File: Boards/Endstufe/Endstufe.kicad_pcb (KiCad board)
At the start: 2 copper layers, 163.6 x 110.2 mm, 60 parts, among them J1 HV In, J2 Relais, J3 NF_In, K1 G6E, P2 Trafo, P4 6V3_AC, P5 Trafo_GK, P6 6V3_DC, P7 VSup1, P8 Bias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

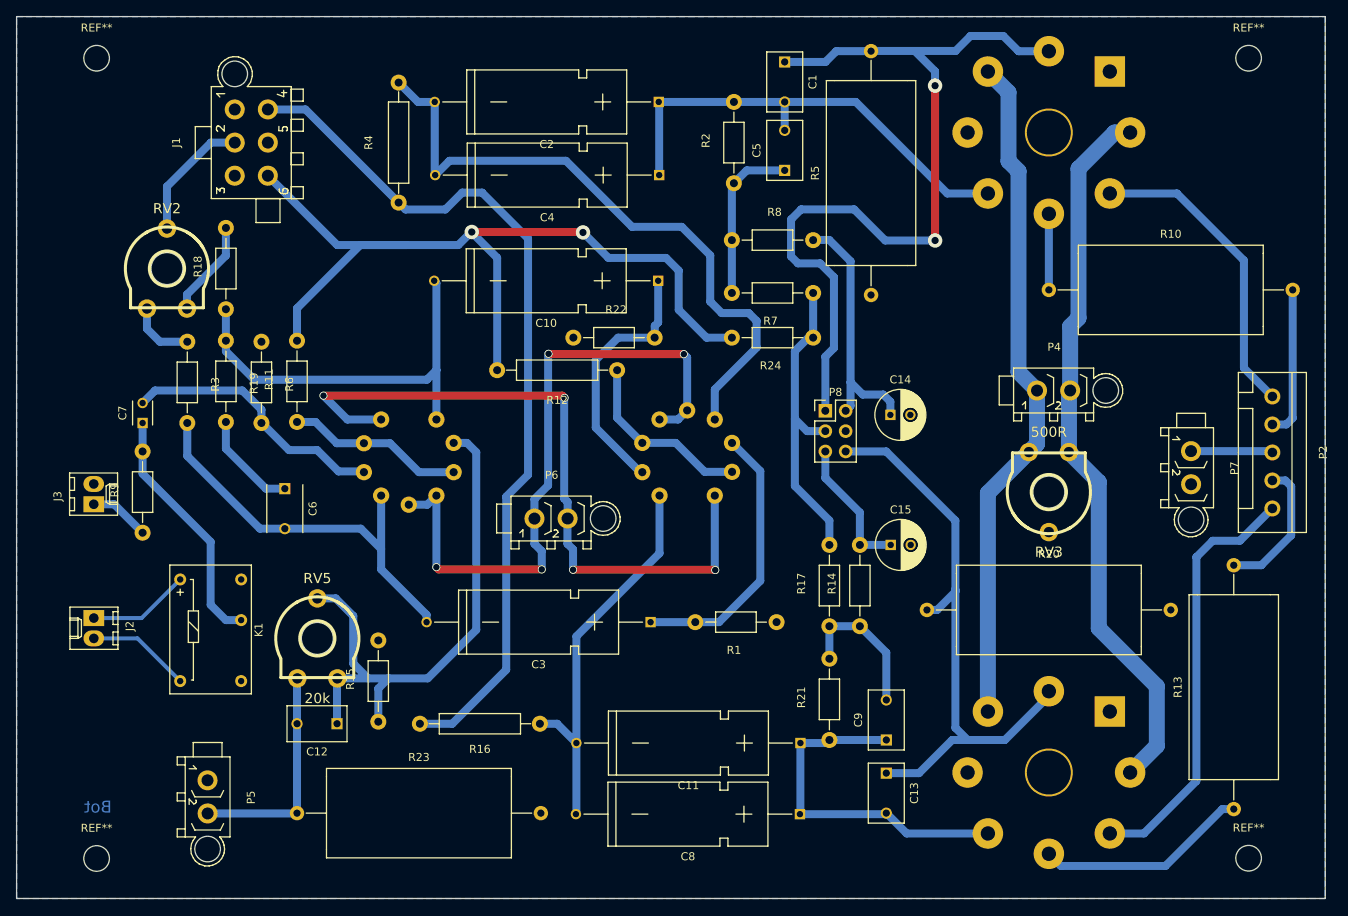
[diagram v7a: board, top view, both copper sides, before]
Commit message: Converted to Kicad 5.1 and Layout changes
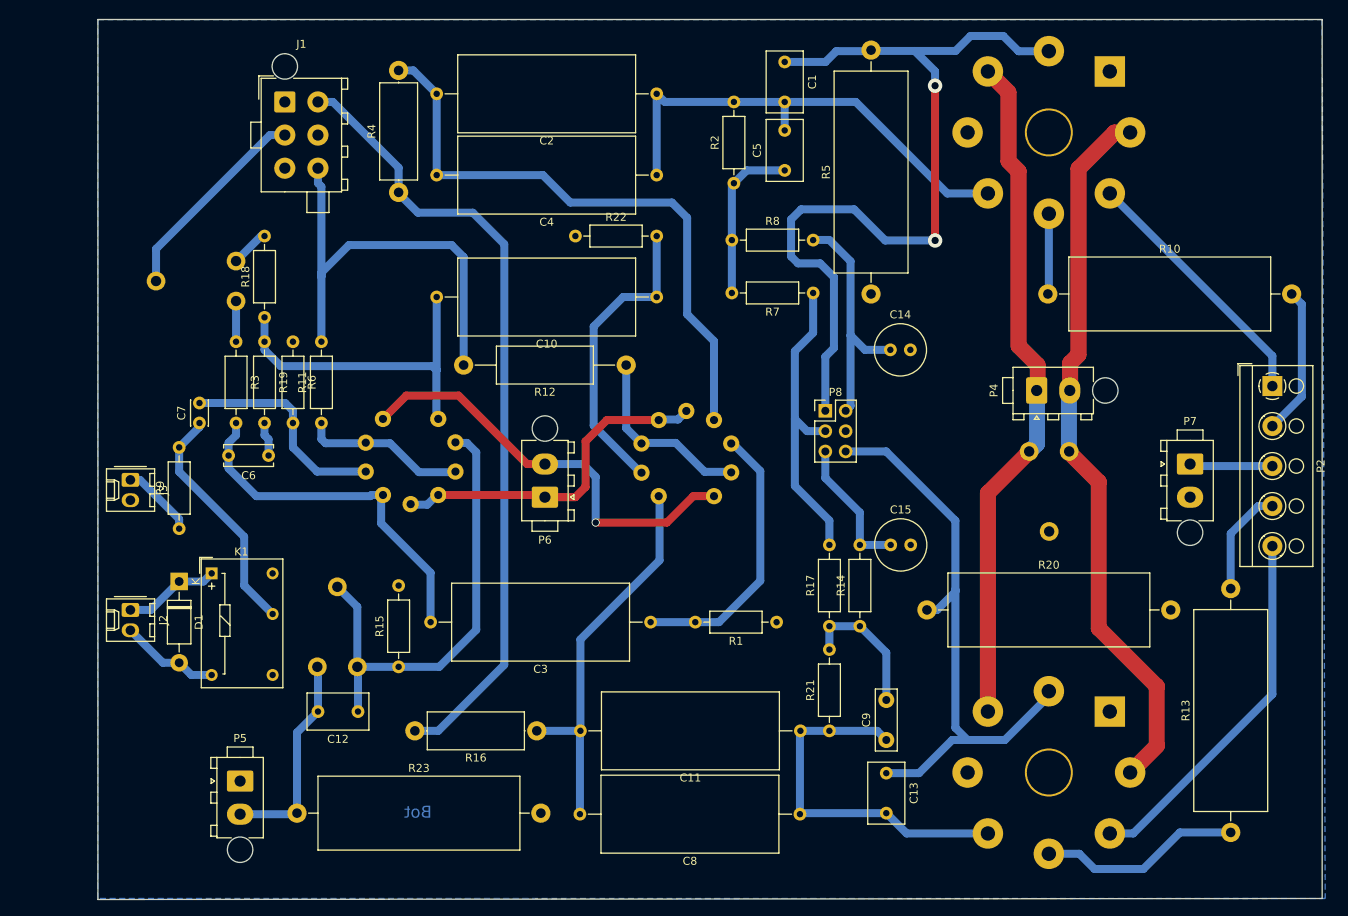
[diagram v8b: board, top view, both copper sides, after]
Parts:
- removed R24: 30k, Resistors_ThroughHole:Resistor_Horizontal_RM10mm
- removed REF** (x4): MountingHole_3.2mm_M3_DIN965, Mounting_Holes:MountingHole_3.2mm_M3_DIN965
- added D1: 1N4001, Diode_THT:D_DO-41_SOD81_P10.16mm_Horizontal, F.Cu at (69.1, 122.4)
- C1, C12, C13, C5: footprint Capacitors_ThroughHole:C_Disc_D7.5_P5 -> Capacitor_THT:C_Disc_D7.5mm_W4.4mm_P5.00mm
- C10, C11, C2, C3, C4, C8: footprint Capacitors_ThroughHole:C_Axial_D8_L21_P28 -> Capacitor_THT:C_Axial_L22.0mm_D9.5mm_P27.50mm_Horizontal
- C14, C15: footprint Capacitors_ThroughHole:C_Radial_D6.3_L11.2_P2.5 -> Capacitor_THT:C_Radial_D6.3mm_H5.0mm_P2.50mm
- C6: footprint Capacitors_ThroughHole:C_Disc_D6_P5 -> Capacitor_THT:C_Disc_D6.0mm_W2.5mm_P5.00mm
- C7: footprint Capacitors_ThroughHole:C_Disc_D3_P2.5 -> Capacitor_THT:C_Disc_D3.0mm_W2.0mm_P2.50mm
- C9: footprint Capacitors_ThroughHole:C_Disc_D7.5_P5 -> Capacitor_THT:C_Disc_D7.5mm_W2.5mm_P5.00mm
- J1: footprint Connectors_Mini-Universal:MiniUniversalMate-N-LokSocket_6PinVertical -> Connector_TE-Connectivity:TE_MATE-N-LOK_1-770875-x_2x03_P4.14mm_Vertical
- J2, J3: footprint Connectors_Molex:Molex_KK-6410-02_02x2.54mm_Straight -> Connector_Molex:Molex_KK-254_AE-6410-02A_1x02_P2.54mm_Vertical
- K1: footprint Relays_THT:Relay_SPDT_OMRON-G6E -> Relay_THT:Relay_SPDT_Omron_G6E
- P2: footprint Sockets_WAGO734:WAGO_734_5pin_Straight -> TerminalBlock_RND:TerminalBlock_RND_205-00004_1x05_P5.00mm_Horizontal
- P4, P5, P6, P7: footprint Sockets_Mini-Universal:MiniUniversalMate-N-LokSocket_2PinVertical -> Connector_TE-Connectivity:TE_MATE-N-LOK_1-770866-x_1x02_P4.14mm_Vertical
- P8: footprint Pin_Headers:Pin_Header_Straight_2x03_Pitch2.54mm -> Connector_PinHeader_2.54mm:PinHeader_2x03_P2.54mm_Vertical
- R1, R11, R14, R15, R17, R18, R19, R2, R21, R22, R3, R6, R7, R8, R9: footprint Resistors_ThroughHole:Resistor_Horizontal_RM10mm -> Resistor_THT:R_Axial_DIN0207_L6.3mm_D2.5mm_P10.16mm_Horizontal
- R10, R13, R20, R23, R5: footprint Resistors_ThroughHole:Resistor_Ceramic_Horizontal_L23mm-W9mm-H9mm-p30mm -> Resistor_THT:R_Axial_Power_L25.0mm_W9.0mm_P30.48mm
- R12: footprint Resistors_ThroughHole:Resistor_Horizontal_RM15mm -> Resistor_THT:R_Axial_DIN0414_L11.9mm_D4.5mm_P20.32mm_Horizontal
- R16, R4: footprint Resistors_ThroughHole:Resistor_Horizontal_RM15mm -> Resistor_THT:R_Axial_DIN0414_L11.9mm_D4.5mm_P15.24mm_Horizontal
- RV2, RV3, RV5: footprint w_pth_resistors:trimmer_piher_pt10xv10 -> Potentiometer_THT:Potentiometer_Piher_PT-10-V10_Vertical; moved to B.Cu
- T1, T2: footprint Valves:VALVE-OCTAL -> Valve:Valve_Octal
- U1, U2: footprint Valves:VALVE-ECC-83-1 -> Valve:Valve_ECC-83-1
- moved R13 18.2 mm to (200.5, 153.8)
- moved R10 15.4 mm to (177.7, 86.5)
- moved R20 15.2 mm to (162.6, 126.0)
- moved R23 15.2 mm to (83.8, 151.4)
- moved R5 15.1 mm to (155.6, 86.5)
- moved R22 13.6 mm to (118.6, 79.2)
- moved T1 10.8 mm to (185.4, 58.7)
- moved T2 10.8 mm to (185.4, 138.7)
- moved RV2 9.54 mm to (76.2, 87.4)
- moved R12 8.66 mm to (125.0, 95.4)
- moved P2 8.30 mm to (205.7, 98.0)
- moved C14 8.13 mm to (158.0, 93.5)
- moved R3 7.94 mm to (76.2, 92.5)
- moved R18 7.78 mm to (79.8, 89.4)
- moved R16 7.17 mm to (113.8, 141.1)
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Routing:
- net -120V: track 110.2 -> 55.7 mm, vias 2 -> 0
- net Net-(P6-Pad1): track 82.3 -> 42.9 mm, vias 4 -> 0
- net Net-(P6-Pad2): track 87.8 -> 53.9 mm, vias 4 -> 1
- net Net-(C12-Pad1): track 71.0 -> 59.0 mm
- net +240V: track 16.0 -> 26.0 mm
- net +300V: track 109.7 -> 99.7 mm
- net Net-(C10-Pad2): track 51.0 -> 41.9 mm
- net Net-(C6-Pad1): track 12.8 -> 4.27 mm
- net Net-(P2-Pad5): track 53.5 -> 46.1 mm
- net Net-(R18-Pad2): track 12.1 -> 4.85 mm
- net Net-(C7-Pad2): track 33.5 -> 27.1 mm
- net Net-(P2-Pad1): track 38.8 -> 32.6 mm
- net Net-(C3-Pad2): track 51.3 -> 45.2 mm
- net Net-(C10-Pad1): track 32.4 -> 37.9 mm
- net Net-(C2-Pad2): track 81.8 -> 76.4 mm
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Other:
- board size 163.6 x 110.2 mm -> 153 x 110 mm
